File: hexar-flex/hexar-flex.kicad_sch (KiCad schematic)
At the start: 204 parts, among them J1 ???, J10 -, J101 Conn_01x04, J11 +, J12 OUT, J13 IN, J14 -, J16 GND, J2 Conn_01x10, J3 DX, J4 Conn_01x02, J5 Conn_01x12_MountingPin, J6 Conn_01x08_MountingPin, J7 +, J8 -, J9 +, Q1 UN2214, Q10 UN2124, Q11 UN2114, Q12 UN2214, Q13 XN1211, Q14 XN1213, Q15 Q_Dual_NPN_C2C1E1E2, Q2 HQ1A4A, Q3 UN2114, Q4 BK, Q5 UN2114, Q6 UN2114, Q7 CR08AS-8, Q8 UN2211, Q9 UN2124, SW1 SW_Push, SW101 SKRNPME010, SW2 SW_Push, SW3 SW_Push, SW4 SW_Push, U1 BR93CS46, U10 Photodiode, U2 M37423M8H-101FP, U3 LB1837M, U4 LB8620M, U5 LB8620M, U6 LDO 3.0V Iq=1.3uA, U7 IR3S64N1/T1, U8 S-8052ANB-NE?, U9 LDO 3.0V Iq=1.3uA, Y1 32768Hz?, Y2 2.00MHz

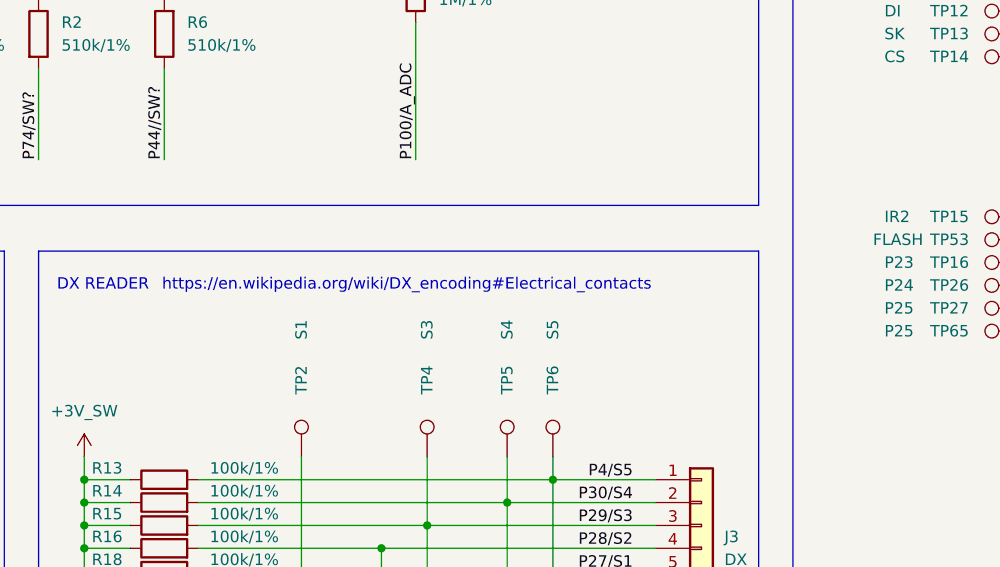
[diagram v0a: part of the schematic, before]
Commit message: update pcb, more documentation and value fixes
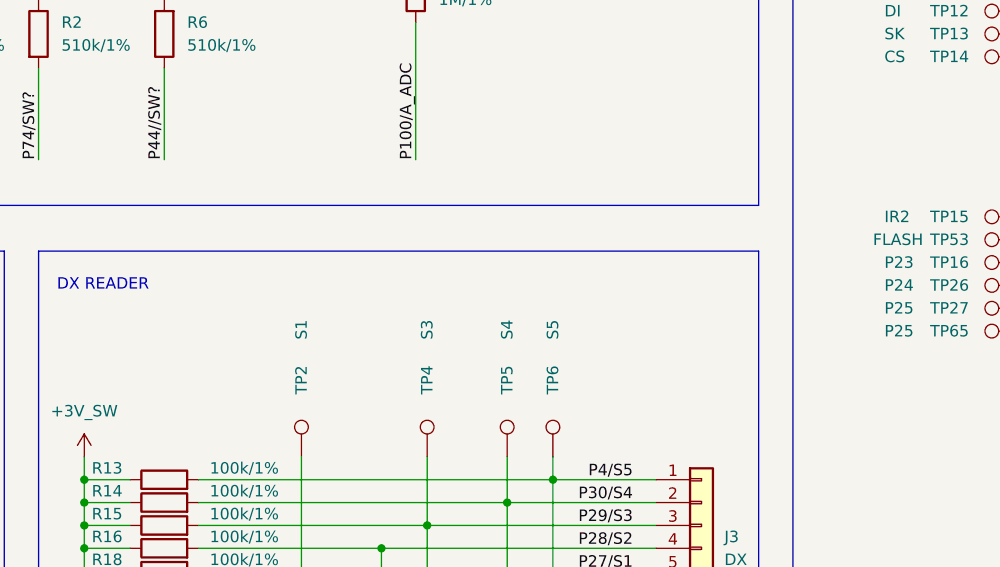
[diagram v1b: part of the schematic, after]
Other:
- note removed: "https://en.wikipedia.org/wiki/DX_encoding#Electrical_contacts"
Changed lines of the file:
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@@
 		)
 	)
-	(text "https://en.wikipedia.org/wiki/DX_encoding#Electrical_contacts"
-		(exclude_from_sim no)
-		(at 124.206 276.352 0)
-		(effects
-			(font
-				(size 1.27 1.27)
-			)
-			(justify left bottom)
-			(href "https://en.wikipedia.org/wiki/DX_encoding#Electrical_contacts")
-		)
-	)
 	(text "DOOR SENSOR"
 		(exclude_from_sim no)
@@
 			)
 		)
-		(property "Datasheet" "~"
+		(property "Datasheet" "https://en.wikipedia.org/wiki/DX_encoding#Electrical_contacts"
 			(at 184.15 304.8 0)
 			(effects

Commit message: WIP (keyboard, PSD)
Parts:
- D7: symbol Device:D_Dual_CommonCathode_AKA -> Device:D_Dual_CommonCathode_AAK
- J2: value Conn_01x10 -> KBD-FLEX; footprint (none) -> flex-smd:HEXAR-KBD-CONNECTOR; now left out of the parts list
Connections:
- net P44//SW? is gone; now on net P44/SW?: R6.1
- net +3V_SW: now also J2.1 (Pin_1); no longer J2.10 (Pin_10)
- net GND: now also J2.3 (Pin_3), J2.9 (Pin_9); no longer J2.2 (Pin_2), J2.8 (Pin_8)
- net P100/A_ADC: now also J2.2 (Pin_2); no longer J2.9 (Pin_9)
- net P44/SW?: now also J2.6 (Pin_6); no longer J2.5 (Pin_5)
- net P67/SW?: now also J2.5 (Pin_5); no longer J2.6 (Pin_6)
- net P68/SW?: now also J2.4 (Pin_4); no longer J2.7 (Pin_7)
- net P35/SW? renamed P35/SW_P
- net P35/SW_P: now also J2.10 (Pin_10); no longer J2.1 (Pin_1)
- net P63/SW? renamed P63/SW_A
- net P63/SW_A: now also J2.7 (Pin_7); no longer J2.4 (Pin_4)
- net P74/SW? renamed P74/SW_M
- net P74/SW_M: now also J2.8 (Pin_8); no longer J2.3 (Pin_3)
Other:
- moved on the sheet: J2
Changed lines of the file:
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@@
 		)
 	)
-	(label "P35{slash}SW?"
+	(label "P35{slash}SW_P"
 		(at 76.2 196.85 180)
 		(fields_autoplaced yes)
@@
 		)
 	)
-	(label "P35{slash}SW?"
+	(label "P35{slash}SW_P"
 		(at 252.73 313.69 90)
 		(fields_autoplaced yes)
@@
 		)
 	)
-	(label "P63{slash}SW?"
+	(label "P63{slash}SW_A"
 		(at 76.2 204.47 180)
 		(fields_autoplaced yes)
@@
 		)
 	)
-	(label "P74{slash}SW?"
+	(label "P74{slash}SW_M"
 		(at 76.2 201.93 180)
 		(fields_autoplaced yes)
@@
 		)
 	)
-	(label "P74{slash}SW?"
+	(label "P74{slash}SW_M"
 		(at 110.49 261.62 90)
 		(fields_autoplaced yes)
@@
 		)
 	)
-	(label "P35{slash}SW?"
-		(at 80.01 207.01 0)
+	(label "P35{slash}SW_P"
+		(at 110.49 214.63 180)
 		(fields_autoplaced yes)
 		(effects
@@
 				(size 1.27 1.27)
 			)
-			(justify left bottom)
+			(justify right bottom)
 		)
 	)
@@
 		)
 	)
-	(label "P63{slash}SW?"
+	(label "P63{slash}SW_A"
 		(at 96.52 261.62 90)
 		(fields_autoplaced yes)
@@
 		)
 	)
-	(label "P44{slash}{slash}SW?"
+	(label "P44{slash}SW?"
 		(at 124.46 261.62 90)
 		(fields_autoplaced yes)
@@
 		)
 	)
-	(label "P74{slash}SW?"
+	(label "P74{slash}SW_M"
 		(at 317.5 232.41 180)
 		(fields_autoplaced yes)
@@
 		)
 	)
-	(label "P63{slash}SW?"
+	(label "P63{slash}SW_A"
 		(at 317.5 260.35 180)
 		(fields_autoplaced yes)
@@
 		)
 	)
-	(label "P74{slash}SW?"
-		(at 110.49 214.63 180)
+	(label "P74{slash}SW_M"
+		(at 80.01 207.01 0)
 		(fields_autoplaced yes)
 		(effects
@@
 				(size 1.27 1.27)
 			)
-			(justify right bottom)
+			(justify left bottom)
 		)
 	)
@@
 		)
 	)
-	(label "P63{slash}SW?"
+	(label "P63{slash}SW_A"
 		(at 110.49 199.39 180)
 		(fields_autoplaced yes)
@@
 		)
 	)
-	(label "P35{slash}SW?"
+	(label "P35{slash}SW_P"
 		(at 82.55 261.62 90)
 		(fields_autoplaced yes)
@@
 	(symbol
 		(lib_id "Connector_Generic:Conn_01x10")
-		(at 48.26 207.01 0)
-		(mirror y)
+		(at 48.26 209.55 180)
 		(unit 1)
 		(exclude_from_sim no)
-		(in_bom yes)
+		(in_bom no)
 		(on_board yes)
 		(dnp no)
@@
 			)
 		)
-		(property "Value" "Conn_01x10"
+		(property "Value" "KBD-FLEX"
 			(at 48.26 193.04 0)
 			(effects
@@
 			)
 		)
-		(property "Footprint" ""
-			(at 48.26 207.01 0)
+		(property "Footprint" "flex-smd:HEXAR-KBD-CONNECTOR"
+			(at 48.26 209.55 0)
 			(effects
 				(font
@@
 			)
 		)
-		(property "Datasheet" "~"
-			(at 48.26 207.01 0)
+		(property "Datasheet" ""
+			(at 48.26 209.55 0)
 			(effects
 				(font
@@
 		)
 		(property "Description" ""
-			(at 48.26 207.01 0)
+			(at 48.26 209.55 0)
 			(effects
 				(font
@@
 	)
 	(symbol
-		(lib_id "Device:D_Dual_CommonCathode_AKA")
+		(lib_id "Device:D_Dual_CommonCathode_AAK")
 		(at 96.52 207.01 270)
 		(unit 1)
@@
 		(fields_autoplaced yes)
 		(property "Reference" "D7"
-			(at 99.06 205.74 90)
+			(at 99.06 205.7399 90)
 			(effects
 				(font
@@
 		)
 		(property "Value" "1SS184"
-			(at 99.06 208.28 90)
+			(at 99.06 208.2799 90)
 			(effects
 				(font
@@
 			)
 		)
-		(property "Datasheet" "https://raw.githubusercontent.com/kosma/hexar-resurrection/main/datasheets/1SS184.pdf"
+		(property "Datasheet" "~"
 			(at 96.52 207.01 0)
 			(effects
@@
 			)
 		)
-		(property "Description" ""
+		(property "Description" "Dual diode, common cathode on pin 3"
 			(at 96.52 207.01 0)
 			(effects

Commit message: WIP (separating grounds)
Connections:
- net GND: no longer C15.2, C16.2, C17.2, C18.2, C2.2, C5.2, C6.2, D101.4 (GND), D102.4 (GND), J2.3 (Pin_3), J2.9 (Pin_9), R10.2, R20.2, R21.2, R22.1, R23.1, R28.2, R29.2, R8.2, SW4.2, U2.36, U2.40 (Vss), U3.12 (GND), U3.9 (GND), U4.1 (FGND), U4.14 (FGND), U4.15 (FGND), U4.16 (FGND), U4.17 (FGND), U4.2 (FGND), U4.23 (GND), U4.29 (FGND), U4.30 (FGND), U5.1 (FGND), U5.14 (FGND), U5.15 (FGND), U5.16 (FGND), U5.17 (FGND), U5.2 (FGND), U5.23 (GND), U5.29 (FGND), U5.30 (FGND), U7.7 (GND)
- new net GNDD: C15.2, C16.2, C17.2, C18.2, C2.2, C5.2, C6.2, D101.4 (GND), D102.4 (GND), J2.3 (Pin_3), J2.9 (Pin_9), R10.2, R20.2, R21.2, R22.1, R23.1, R28.2, R29.2, R8.2, SW4.2, U2.36, U2.40 (Vss), U7.7 (GND)
- new net GNDPWR: U3.12 (GND), U3.9 (GND), U4.1 (FGND), U4.15 (FGND), U4.16 (FGND), U4.17 (FGND), U4.2 (FGND), U4.23 (GND), U4.29 (FGND), U4.30 (FGND), U5.1 (FGND), U5.14 (FGND), U5.15 (FGND), U5.16 (FGND), U5.17 (FGND), U5.2 (FGND), U5.23 (GND), U5.29 (FGND), U5.30 (FGND)
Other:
- note added: "TODO: IR has its own BATT/GND circuit"
- moved on the sheet: C8, C9, D5, Q2, R20, R21, R22, R23, R28, R29, R31, R37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
